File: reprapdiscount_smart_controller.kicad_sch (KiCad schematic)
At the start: 17 parts, among them Q1 BC817, U1 74HC4050, U2 MIC5209

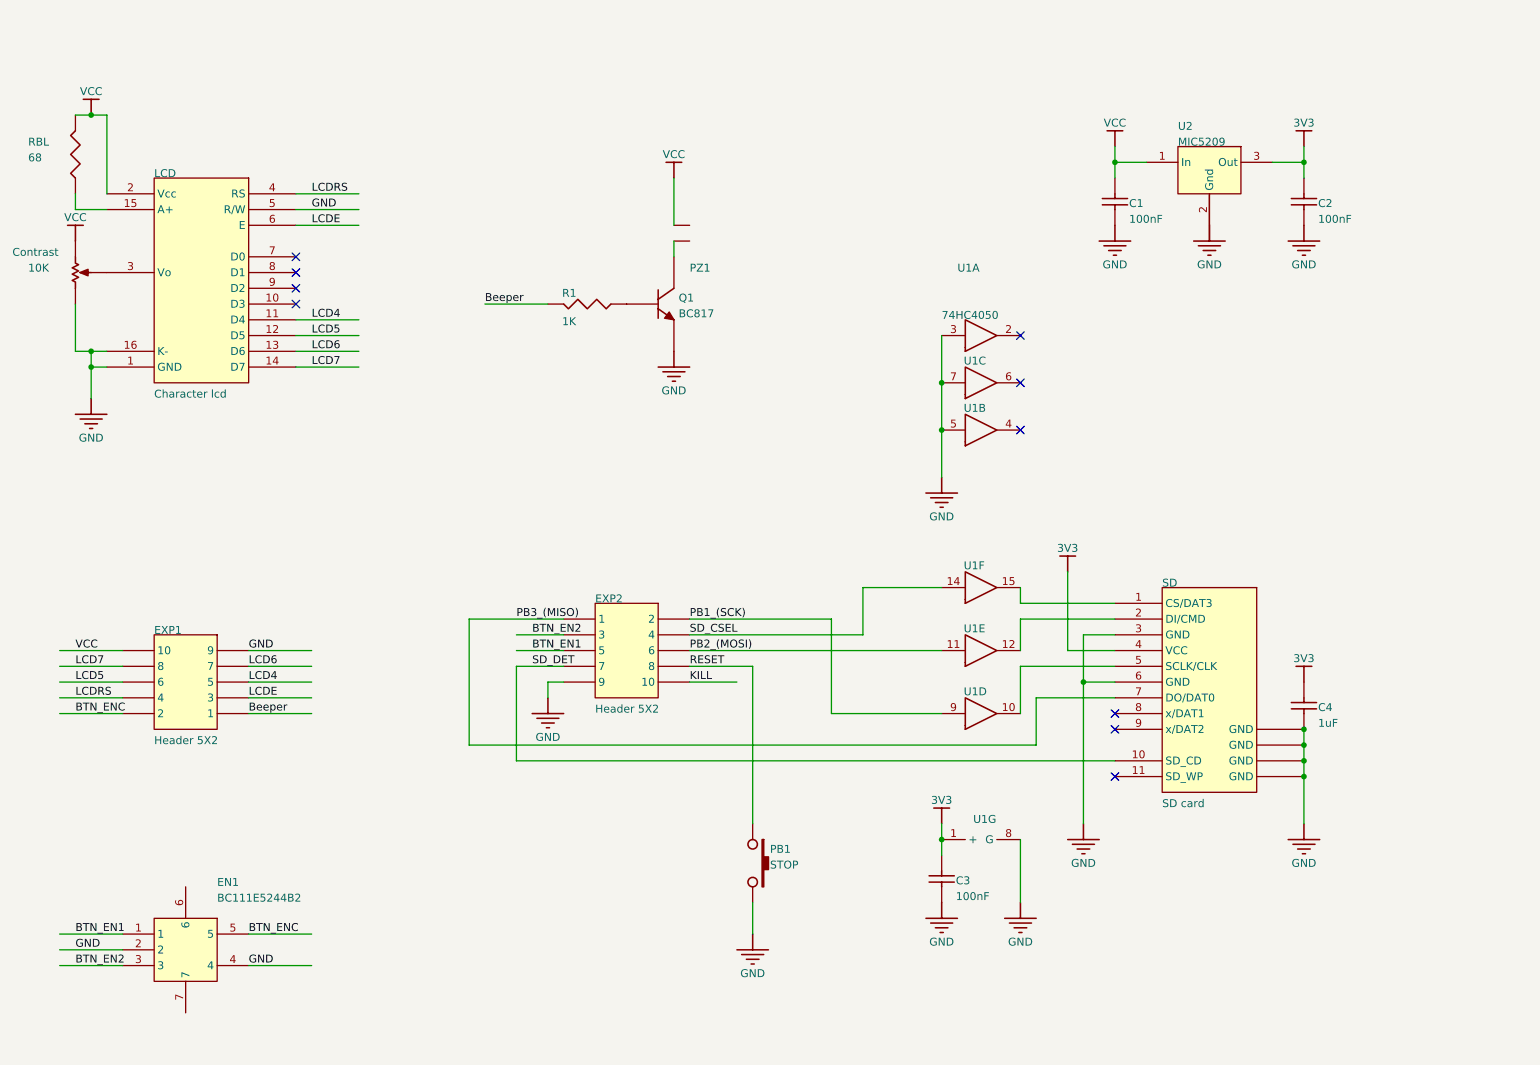
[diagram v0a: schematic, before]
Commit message: fixup: fix schematic and layout references
- replace random 3V3 pth footprints with vias
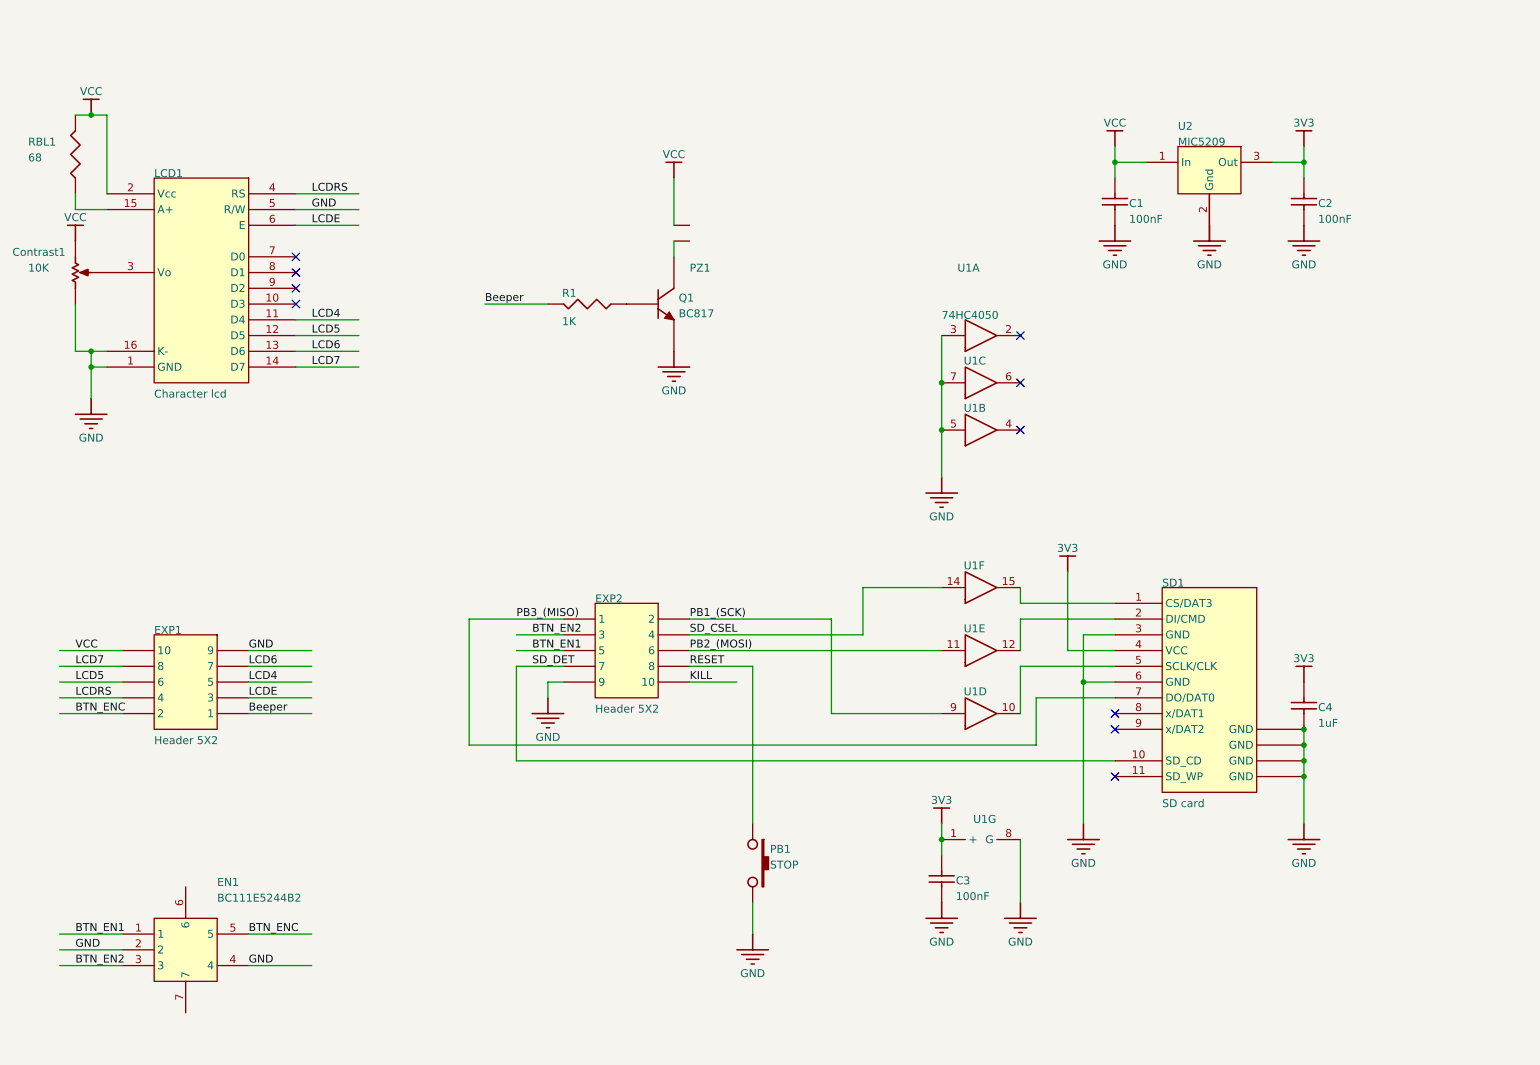
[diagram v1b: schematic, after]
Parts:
- C1, C2, C3: footprint Cap2012-0805 -> reprapdiscount_smart_controller:Cap2012-0805
- C4: footprint Cap3216-1206 -> reprapdiscount_smart_controller:Cap3216-1206
- Contrast1: renamed from Contrast; footprint RES trimpot -> reprapdiscount_smart_controller:RES TRIMPOT
- EN1: footprint Rotary encoder -> reprapdiscount_smart_controller:ROTARY ENCODER
- EXP1, EXP2: footprint HDR2X5_exp -> reprapdiscount_smart_controller:HDR2X5_EXP
- LCD1: renamed from LCD; footprint HDR1X16 -> reprapdiscount_smart_controller:HDR1X16
- PB1: footprint SW 6x6mm -> reprapdiscount_smart_controller:SW 6X6MM
- PZ1: footprint PIEZO 11mm -> reprapdiscount_smart_controller:PIEZO 11MM
- Q1: footprint SOT23_L -> reprapdiscount_smart_controller:SOT23_L
- R1: footprint Res 2012-0805 -> reprapdiscount_smart_controller:Res 2012-0805
- RBL1: renamed from RBL; footprint Res 3216-1206 -> reprapdiscount_smart_controller:Res 3216-1206
- SD1: renamed from SD; footprint SD_card socket -> reprapdiscount_smart_controller:SD_card socket
- U1: footprint SO16N -> reprapdiscount_smart_controller:SO16N
- U2: footprint SOT-223 -> reprapdiscount_smart_controller:SOT-223

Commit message: fixup: switch to global net names
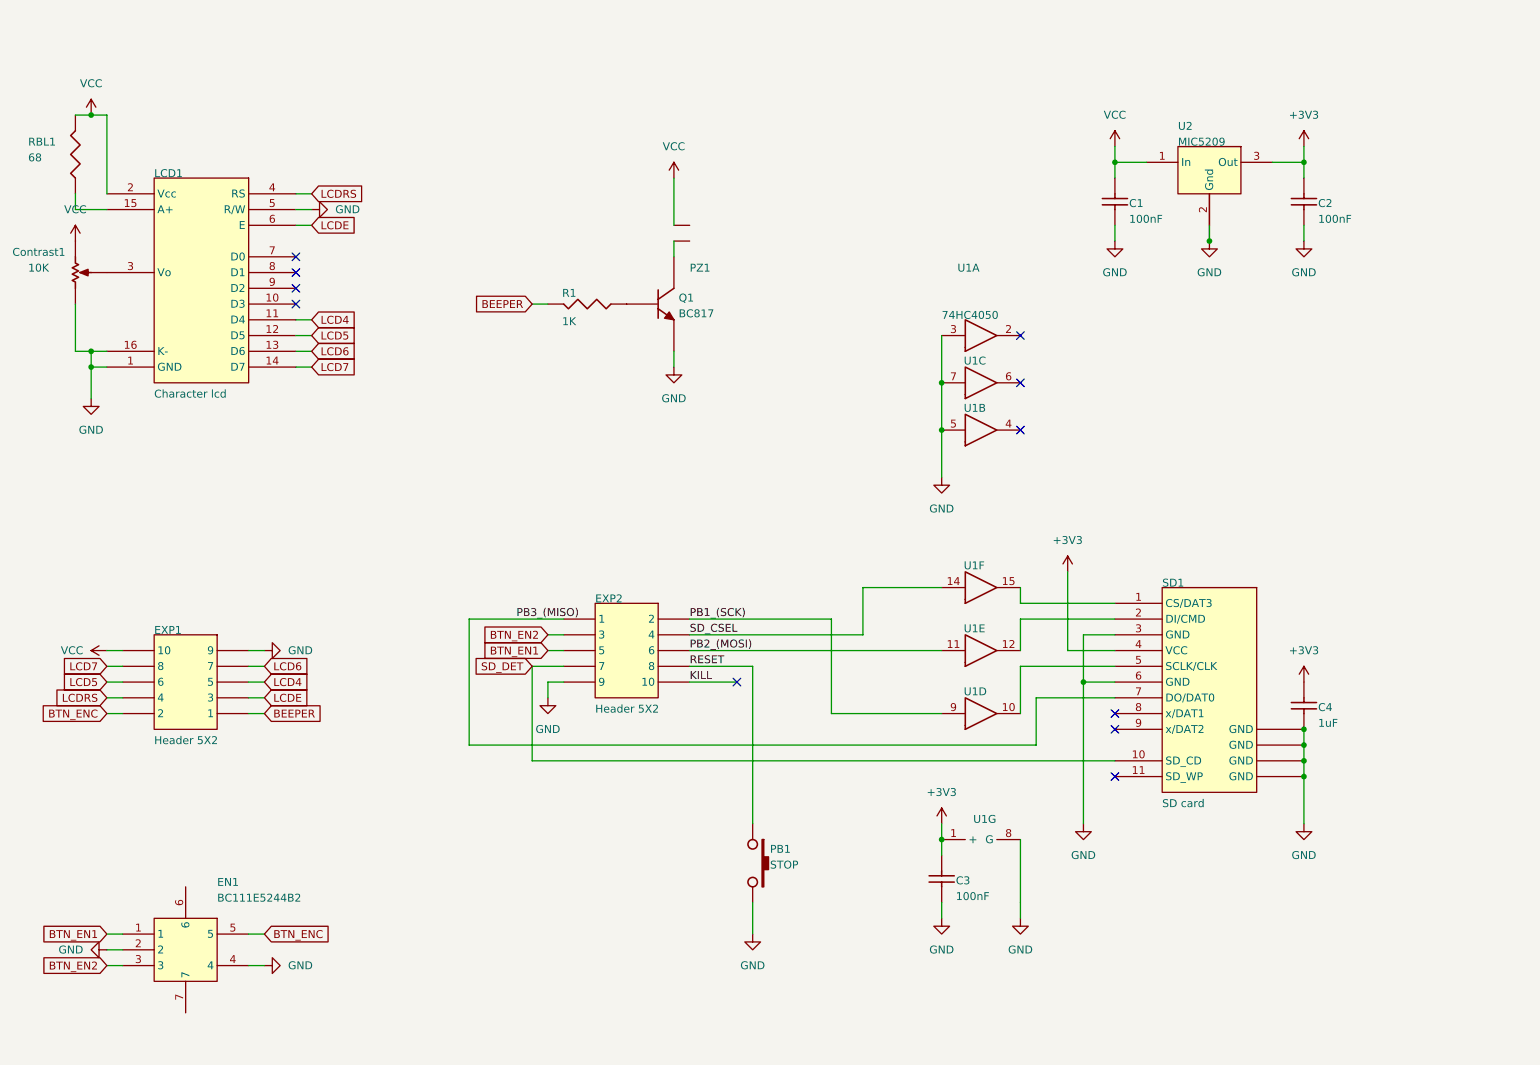
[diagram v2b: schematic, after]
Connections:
- net GND: now also U2.4 (Gnd)
- net 3V3 renamed +3V3
- net Beeper renamed BEEPER
- no-connect marks 10 -> 11

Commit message: fixup: switch to kicad native passive symbols
- redo fill, cleanup broken connections
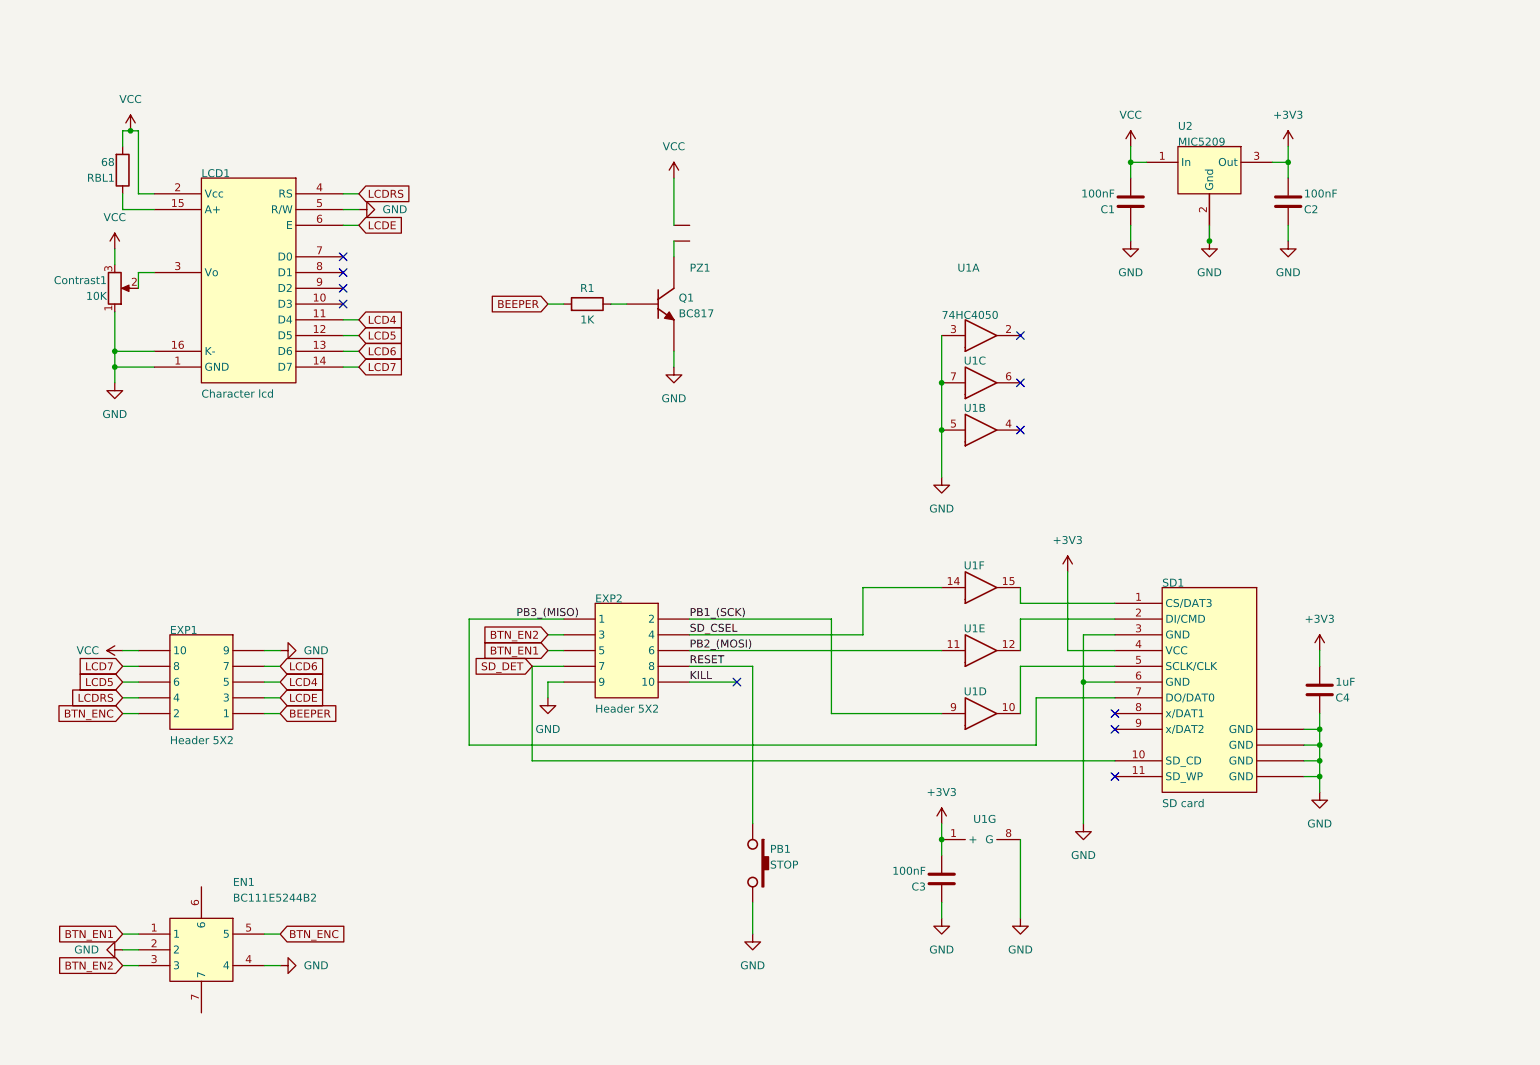
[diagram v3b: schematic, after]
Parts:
- C1, C2, C3, C4: symbol reprapdiscount_smart_controller-altium-import:root_1_Cap Semi -> Device:C
- Contrast1: symbol reprapdiscount_smart_controller-altium-import:root_2_POT -> Device:R_Potentiometer
- R1: symbol reprapdiscount_smart_controller-altium-import:root_2_Res3 -> Device:R
- RBL1: symbol reprapdiscount_smart_controller-altium-import:root_1_Res3 -> Device:R
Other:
- moved on the sheet: EN1, EXP1, LCD1, R1, RBL1

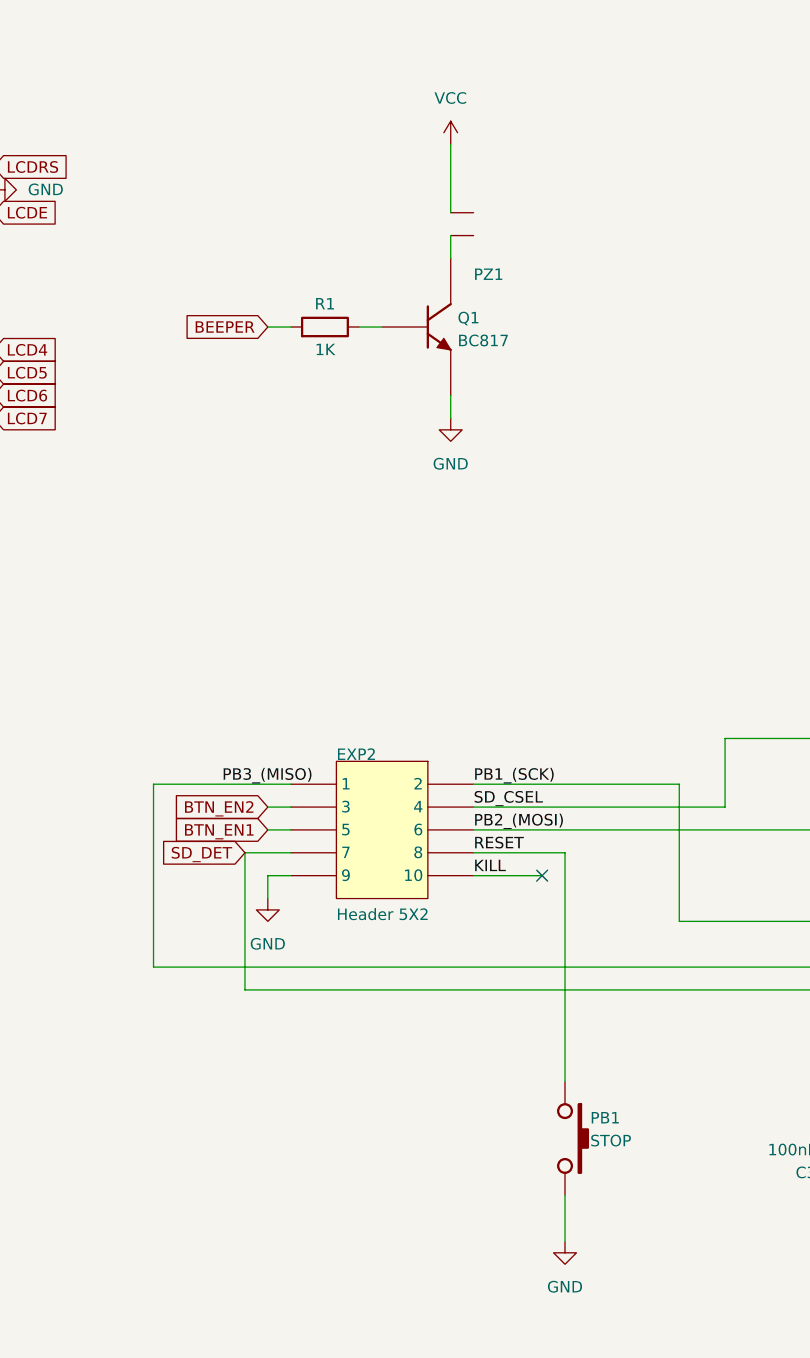
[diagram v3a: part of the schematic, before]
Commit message: fixup: add all missing 3d models
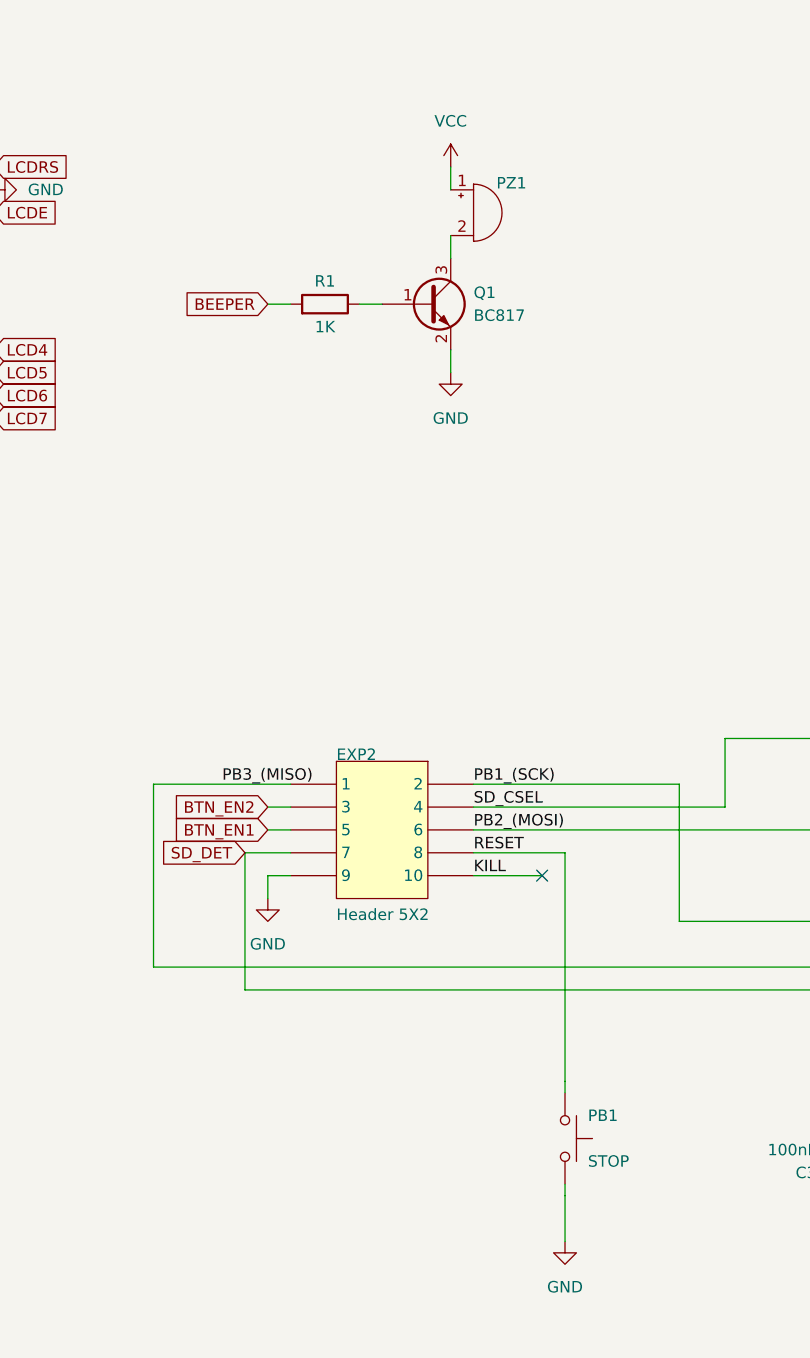
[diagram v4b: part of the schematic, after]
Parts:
- C1, C2, C3: footprint reprapdiscount_smart_controller:Cap2012-0805 -> Capacitor_SMD:C_0805_2012Metric_Pad1.18x1.45mm_HandSolder
- C4: footprint reprapdiscount_smart_controller:Cap3216-1206 -> Capacitor_SMD:C_1206_3216Metric_Pad1.33x1.80mm_HandSolder
- PB1: footprint reprapdiscount_smart_controller:SW 6X6MM -> Button_Switch_THT:SW_PUSH_6mm_H5mm; symbol reprapdiscount_smart_controller-altium-import:root_3_SW-PB -> Switch:SW_Push
- PZ1: symbol reprapdiscount_smart_controller-altium-import:root_2_mirrored_PIEZO -> Device:Buzzer
- Q1: footprint reprapdiscount_smart_controller:SOT23_L -> Package_TO_SOT_SMD:SOT-23; symbol reprapdiscount_smart_controller-altium-import:root_0_BC847C -> Transistor_BJT:BC817
- R1: footprint reprapdiscount_smart_controller:Res 2012-0805 -> Resistor_SMD:R_0805_2012Metric_Pad1.20x1.40mm_HandSolder
- RBL1: footprint reprapdiscount_smart_controller:Res 3216-1206 -> Resistor_SMD:R_1206_3216Metric_Pad1.30x1.75mm_HandSolder
- U1: footprint reprapdiscount_smart_controller:SO16N -> reprapdiscount_smart_controller:SO-16_3.9x9.9mm_P1.27mm
- U2: footprint reprapdiscount_smart_controller:SOT-223 -> Package_TO_SOT_SMD:SOT-223
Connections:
- net VCC: now also PZ1.1 (-); no longer PZ1.2
- net at Q1.3 (C): now also PZ1.2 (+); no longer PZ1.1
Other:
- moved on the sheet: PB1, R1
